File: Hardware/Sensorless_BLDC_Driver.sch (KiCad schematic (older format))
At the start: 27 parts

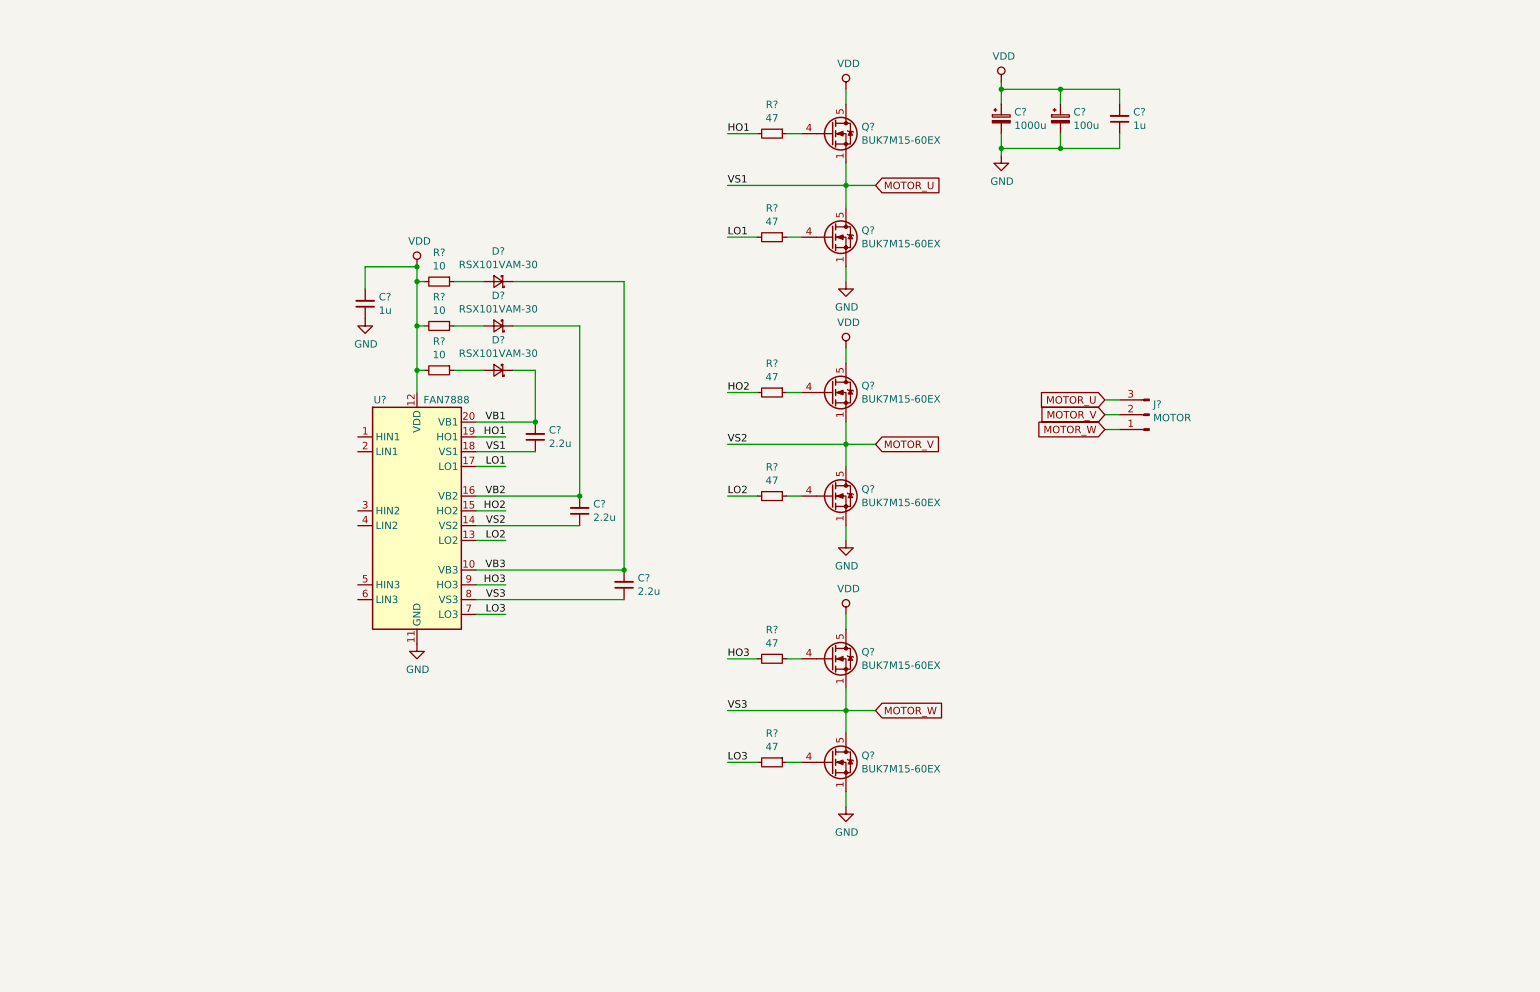
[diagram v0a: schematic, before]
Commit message: [add] add u-controller
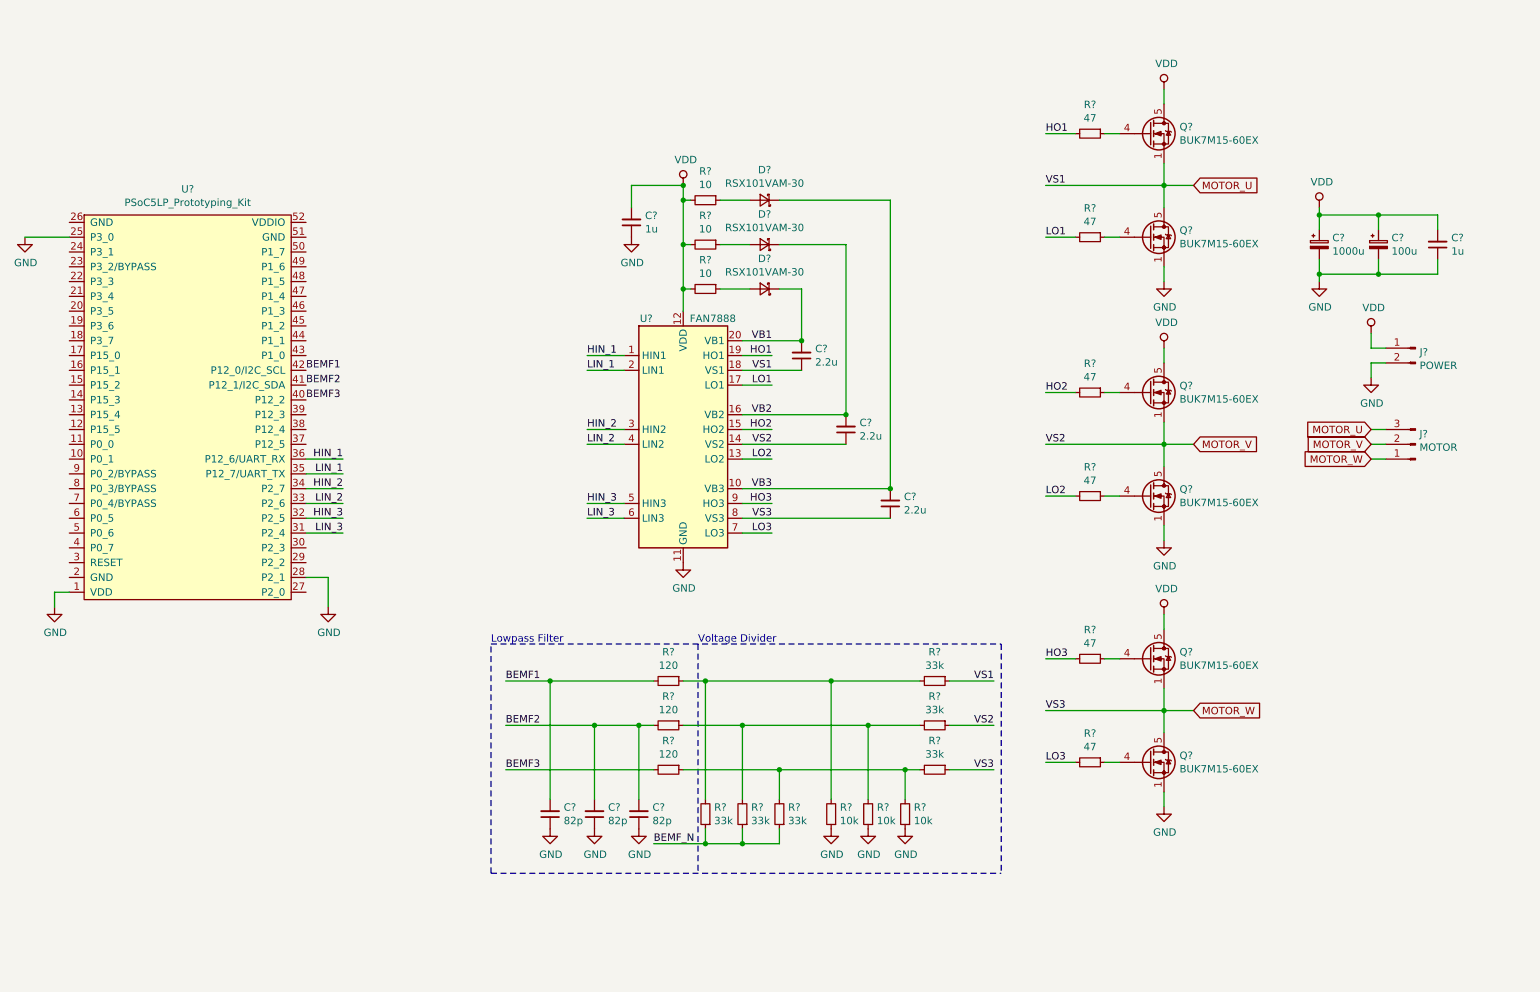
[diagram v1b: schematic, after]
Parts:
- added C? (x3): 82p, symbol Device:C_Small
- added J?: POWER, symbol Connector:Conn_01x02_Male
- added R? (x6): 33k, symbol Device:R_Small
- added R? (x3): 10k, symbol Device:R_Small
- added R? (x3): 120, symbol Device:R_Small
- added U?: PSoC5LP_Prototyping_Kit, symbol KUTKiCad_symbol:PSoC5LP_Prototyping_Kit
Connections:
- net GND: now also C?.1, C?.1, C?.1, J?.2 (Pin_2), R?.1, R?.1, R?.1, U?.1 (VDD), U?.25 (P3_0), U?.28 (P2_1)
- net MOTOR_U: now also R?.1
- net MOTOR_V: now also R?.1
- net MOTOR_W: now also R?.1
- net VDD: now also J?.1 (Pin_1)
- net HIN_1: now reaches U?.1 (HIN1)
- net HIN_1: now also U?.36 (P12_6/UART_RX)
- net LIN_1: now reaches U?.2 (LIN1)
- net LIN_1: now also U?.35 (P12_7/UART_TX)
- net HIN_2: now reaches U?.3 (HIN2)
- net HIN_2: now also U?.34 (P2_7)
- net LIN_2: now reaches U?.4 (LIN2)
- net LIN_2: now also U?.33 (P2_6)
- net HIN_3: now reaches U?.5 (HIN3)
- net HIN_3: now also U?.32 (P2_5)
- net LIN_3: now reaches U?.6 (LIN3)
- net LIN_3: now also U?.31 (P2_4)
- new net: R?.1, R?.2, R?.2, R?.2 (x3)
- new net BEMF1: C?.2, R?.2, U?.42 (P12_0/I2C_SCL)
- new net BEMF2: C?.2, C?.2, R?.2, U?.41 (P12_1/I2C_SDA)
- new net BEMF3: R?.2, U?.40 (P12_2)
- new net BEMF_N: R?.1, R?.1, R?.1
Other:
- note added: "Lowpass Filter"
- note added: "Voltage Divider\n"
- moved on the sheet: C?, D?, J?, Q?, R?, U?

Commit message: [add] add 3-phased current sense
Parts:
- added C? (x3): 0.1u, symbol Device:C_Small
- added R? (x3): 2m, symbol Device:R_Small
- added R? (x6): 4.7, symbol Device:R_Small
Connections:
- net BEMF2: no longer C?.2
- net BEMF3: now also C?.2
- net BEMF_N: now also U?.39 (P12_3)
- net GND: now also R?.1, R?.1, R?.1, R?.1, R?.1, R?.1; no longer Q?.1 (S), Q?.1 (S), Q?.1 (S), Q?.2 (S), Q?.2 (S), Q?.2 (S), Q?.3 (S), Q?.3 (S), Q?.3 (S)
- net ISL_3: now reaches U?.47 (P1_4)
- net ISL_3: now also C?.1, R?.2
- net ISH_3: now reaches U?.48 (P1_5)
- net ISH_3: now also C?.2, R?.2
- net ISL_2: now reaches U?.49 (P1_6)
- net ISL_2: now also C?.1, R?.2
- net ISH_2: now reaches U?.50 (P1_7)
- net ISH_2: now also C?.2, R?.2
- net ISL_1: now reaches U?.51 (GND)
- net ISL_1: now also C?.1, R?.2
- net ISH_1: now reaches U?.52 (VDDIO)
- net ISH_1: now also C?.2, R?.2
- new net: Q?.1 (S), Q?.2 (S), Q?.3 (S), R?.1, R?.2 (x3)
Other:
- moved on the sheet: C?, J?, Q?, R?, U?

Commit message: [update] anotated
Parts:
- added D1: Red, symbol Device:LED_Small
- added D2, D4, D6: Orange, symbol Device:LED_Small
- added D3, D5, D7: Green, symbol Device:LED_Small
- added R1, R2, R4, R6: 4.7k, symbol Device:R_Small
- added R3, R5, R7: 10k, symbol Device:R_Small
- gave numbers to parts that had none: 56
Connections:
- net GND: now also D1.1 (K)
- net MOTOR_U: now also D3.1 (K), D6.1 (K), R2.2, R7.2
- net MOTOR_V: now also D2.1 (K), D5.1 (K), R3.2, R4.2
- net MOTOR_W: now also D4.1 (K), D7.1 (K), R5.2, R6.2
- net VDD: now also R1.2
- new net: D1.2 (A), R1.1
- new net: D2.2 (A), R2.1
- new net: D3.2 (A), R3.1
- new net: D4.2 (A), R4.1
- new net: D5.2 (A), R5.1
- new net: D6.2 (A), R6.1
- new net: D7.2 (A), R7.1
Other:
- moved on the sheet: C1, C10, C11, C12, C13, C2, C3, C4, C5, C6, C7, C8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

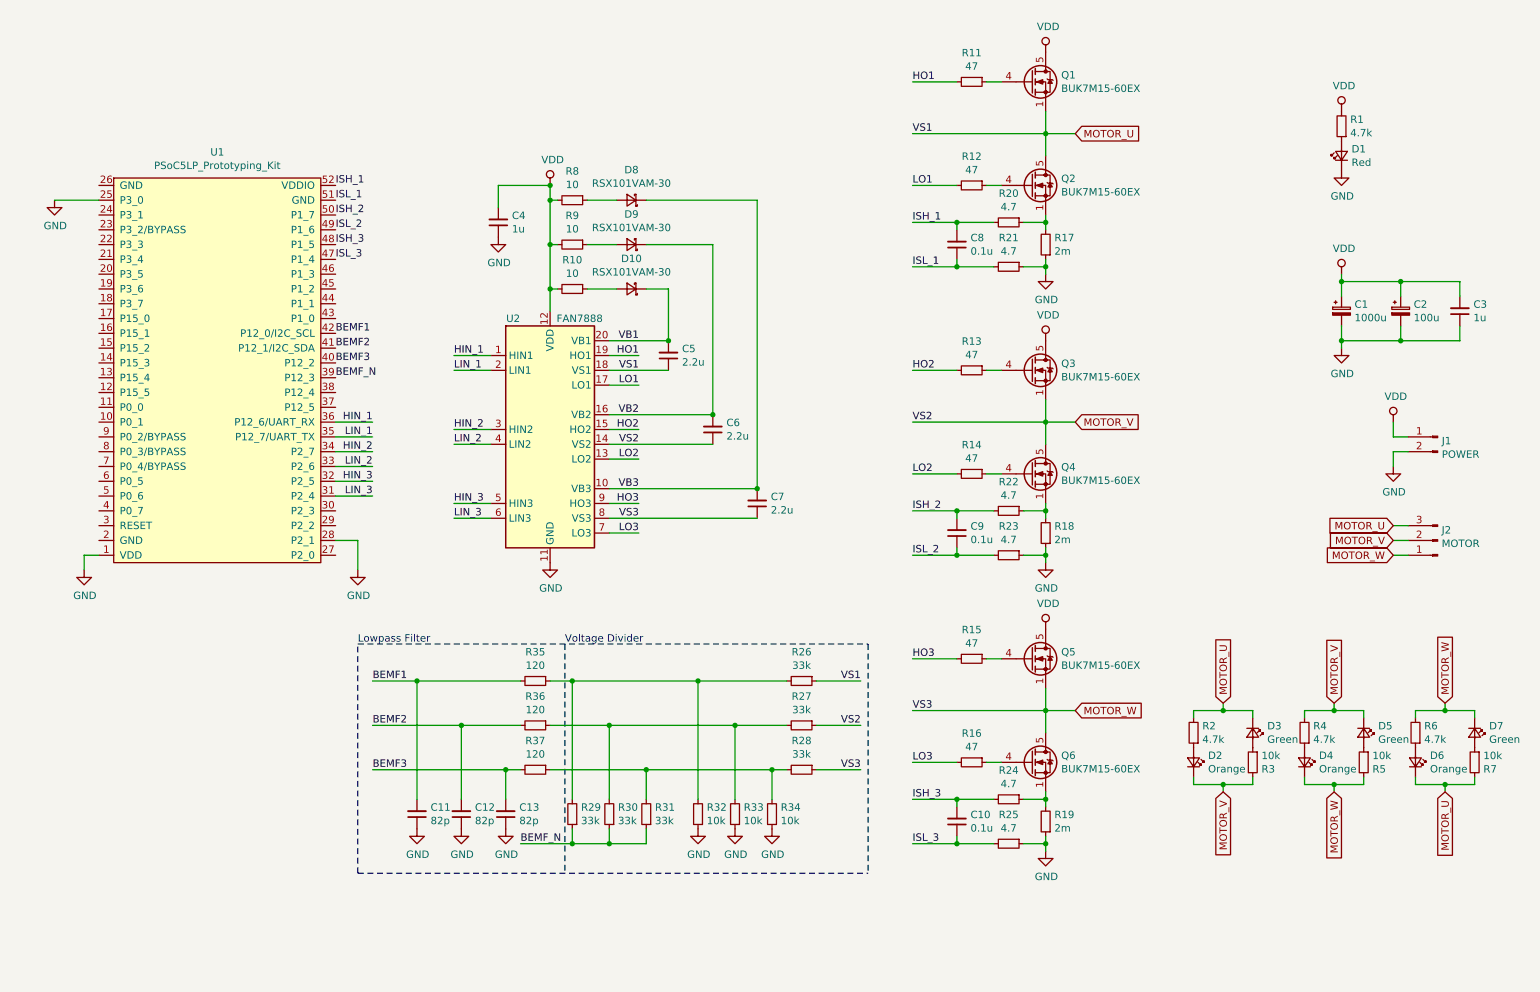
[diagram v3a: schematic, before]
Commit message: [add] Current Sense
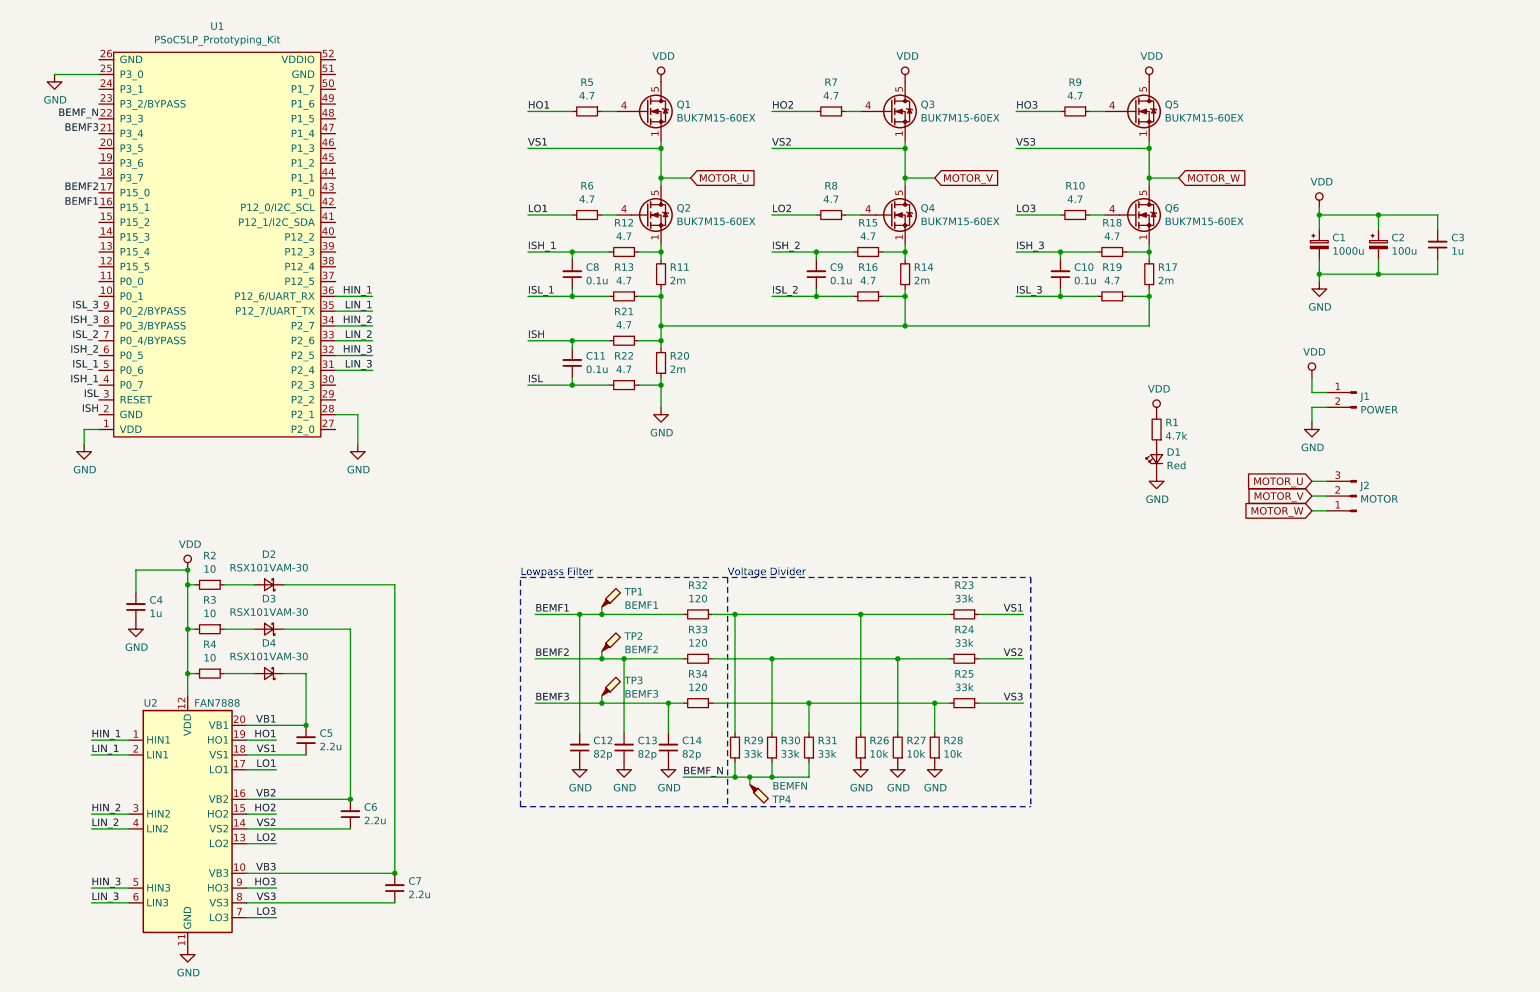
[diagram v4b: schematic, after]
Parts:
- removed D2, D4, D6: Orange, symbol Device:LED_Small
- removed D3, D5, D7: Green, symbol Device:LED_Small
- removed R2, R4, R6: 4.7k, symbol Device:R_Small
- removed R3, R5, R7: 10k, symbol Device:R_Small
- added C11: 0.1u, symbol Device:C_Small
- added R13, R22: 4.7, symbol Device:R_Small
- added R20: 2m, symbol Device:R_Small
- added TP1: BEMF1, TestPoint:TestPoint_THTPad_D1.0mm_Drill0.5mm, symbol Connector:TestPoint_Probe
- added TP2: BEMF2, TestPoint:TestPoint_THTPad_D1.0mm_Drill0.5mm, symbol Connector:TestPoint_Probe
- added TP3: BEMF3, TestPoint:TestPoint_THTPad_D1.0mm_Drill0.5mm, symbol Connector:TestPoint_Probe
- added TP4: BEMFN, TestPoint:TestPoint_THTPad_D1.0mm_Drill0.5mm, symbol Connector:TestPoint_Probe
- R10: renamed from R16; value 47 -> 4.7
- R5: renamed from R11; value 47 -> 4.7
- R6: renamed from R12; value 47 -> 4.7
- R7: renamed from R13; value 47 -> 4.7
- R8: renamed from R14; value 47 -> 4.7
- R9: renamed from R15; value 47 -> 4.7
- renumbered C11 to C12, C12 to C13, C13 to C14, D8 to D2, D9 to D3, D10 to D4, R17 to R11, R20 to R12, R18 to R14, R22 to R15, R23 to R16, R19 to R17, R24 to R18, R25 to R19, R8 to R2, R26 to R23, R27 to R24, R28 to R25, R34 to R26, R33 to R27, R32 to R28, R31 to R29, R9 to R3, R29 to R31, R35 to R32, R36 to R33, R37 to R34, R10 to R4
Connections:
- net BEMF1: now also U1.16 (P15_1), TP1.1; no longer U1.42 (P12_0/I2C_SCL)
- net BEMF2: now also U1.17 (P15_0), TP2.1; no longer U1.41 (P12_1/I2C_SDA)
- net BEMF3: now also U1.21 (P3_4), TP3.1; no longer U1.40 (P12_2)
- net BEMF_N: now also U1.22 (P3_3), TP4.1; no longer U1.39 (P12_3)
- net GND: now also R20.1, R22.1; no longer R11.1, R14.1, R16.1, R17.1, R19.1, R21.1
- net ISH_1: now also U1.4 (P0_7); no longer U1.52 (VDDIO)
- net ISH_2: now also U1.6 (P0_5); no longer U1.50 (P1_7)
- net ISH_3: now also U1.8 (P0_3/BYPASS); no longer U1.48 (P1_5)
- net ISL_1: now also U1.5 (P0_6), R13.2; no longer R21.2, U1.51 (GND)
- net ISL_2: now also U1.7 (P0_4/BYPASS); no longer U1.49 (P1_6)
- net ISL_3: now also U1.9 (P0_2/BYPASS); no longer U1.47 (P1_4)
- net ISH: now reaches U1.2 (GND)
- net ISH: now also R21.2, C11.2
- net ISL: now reaches U1.3 (RESET)
- net ISL: now also C11.1, R22.2
- net at R23.2, R32.1: now also R26.2, R29.2; no longer R28.2, R31.2
- net at R25.2, R34.1: now also R28.2, R31.2; no longer R26.2, R29.2
- new net: R11.1, R13.1, R14.1, R16.1, R17.1, R19.1, R20.2, R21.1
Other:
- moved on the sheet: C1, C10, C12, C13, C14, C2, C3, C4, C5, C6, C7, C8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
